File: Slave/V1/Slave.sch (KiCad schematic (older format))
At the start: 0 parts

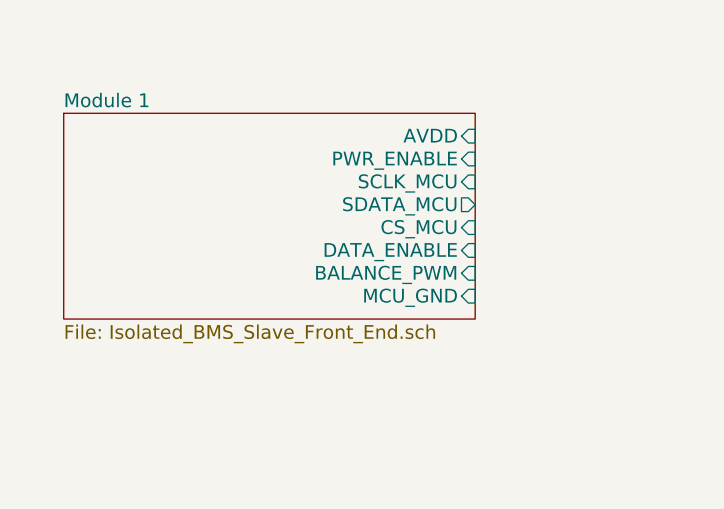
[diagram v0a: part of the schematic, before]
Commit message: add LED to reverse protection + balancing
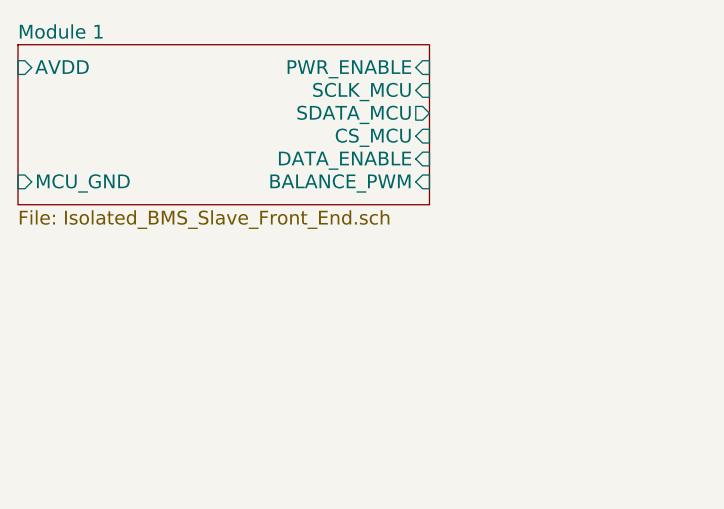
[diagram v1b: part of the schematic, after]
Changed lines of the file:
@@
 	8700 6400 9000 6400
 $Sheet
-S 800  900  1800 900
+S 600  600  1800 700
 U 5938E2BF
 F0 "Module 1" 60
 F1 "Isolated_BMS_Slave_Front_End.sch" 60
-F2 "PWR_ENABLE" I R 2600 1100 60
-F3 "SCLK_MCU" I R 2600 1200 60
-F4 "CS_MCU" I R 2600 1400 60
-F5 "BALANCE_PWM" I R 2600 1600 60
-F6 "SDATA_MCU" O R 2600 1300 60
-F7 "MCU_GND" I R 2600 1700 60
-F8 "DATA_ENABLE" I R 2600 1500 60
-F9 "AVDD" I R 2600 1000 60
+F2 "PWR_ENABLE" I R 2400 700 60
+F3 "SCLK_MCU" I R 2400 800 60
+F4 "CS_MCU" I R 2400 1000 60
+F5 "BALANCE_PWM" I R 2400 1200 60
+F6 "SDATA_MCU" O R 2400 900 60
+F7 "MCU_GND" I L 600 1200 60
+F8 "DATA_ENABLE" I R 2400 1100 60
+F9 "AVDD" I L 600 700 60
 $EndSheet
 $EndSCHEMATC

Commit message: placing components
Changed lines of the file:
@@
 F5 "BALANCE_PWM" I R 2400 1200 60
 F6 "SDATA_MCU" O R 2400 900 60
-F7 "MCU_GND" I L 600 1200 60
-F8 "DATA_ENABLE" I R 2400 1100 60
-F9 "AVDD" I L 600 700 60
+F7 "DATA_ENABLE" I R 2400 1100 60
+F8 "AVDD" I L 600 700 60
+F9 "AGND" I L 600 1200 60
 $EndSheet
 $EndSCHEMATC

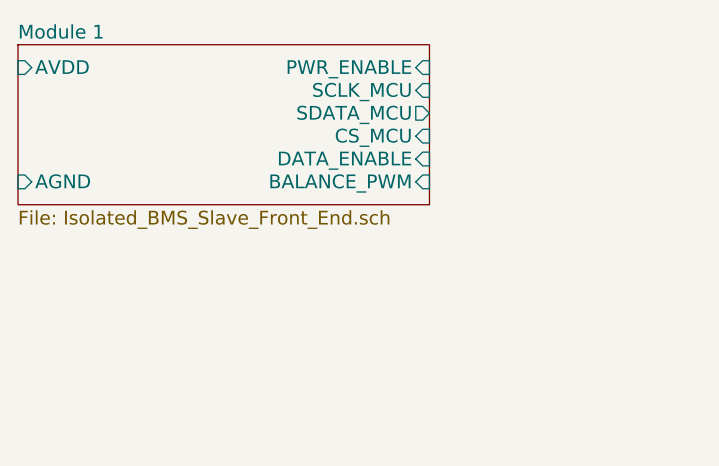
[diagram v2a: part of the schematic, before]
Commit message: placing component on front end
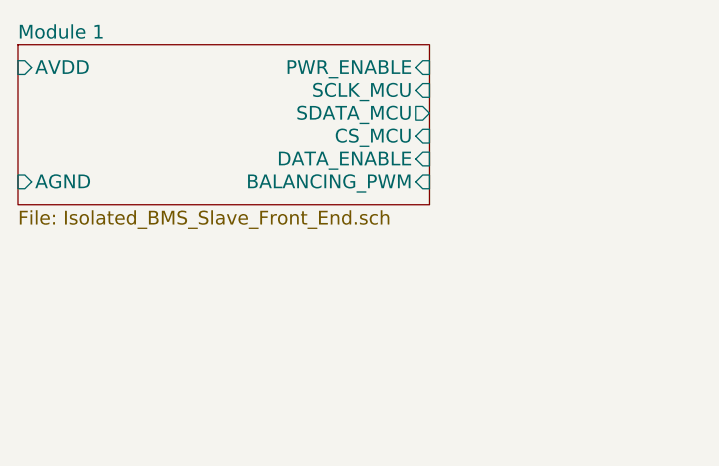
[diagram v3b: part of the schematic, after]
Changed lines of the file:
@@
 F3 "SCLK_MCU" I R 2400 800 60
 F4 "CS_MCU" I R 2400 1000 60
-F5 "BALANCE_PWM" I R 2400 1200 60
+F5 "BALANCING_PWM" I R 2400 1200 60
 F6 "SDATA_MCU" O R 2400 900 60
 F7 "DATA_ENABLE" I R 2400 1100 60

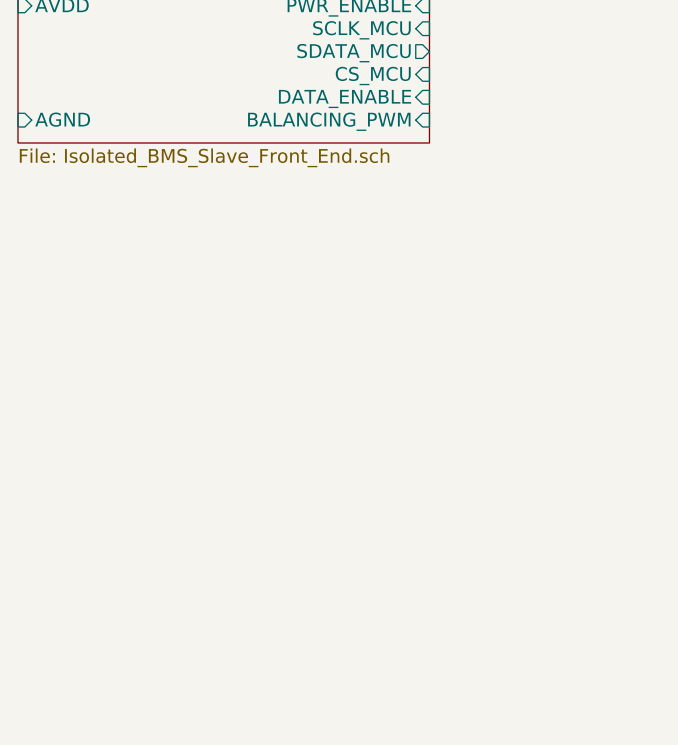
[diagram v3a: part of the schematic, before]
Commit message: adding 8 front end
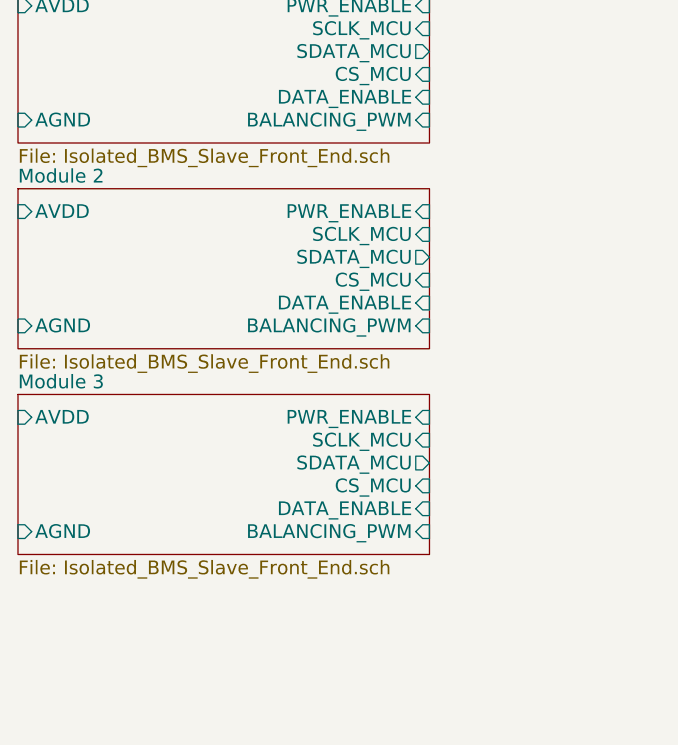
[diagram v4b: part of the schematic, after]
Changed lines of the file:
@@
 $Descr USLetter 11000 8500
 encoding utf-8
-Sheet 1 8
+Sheet 1 16
 Title ""
 Date ""
@@
 F9 "AGND" I L 600 1200 60
 $EndSheet
+$Sheet
+S 600  1500 1800 700
+U 593F9F72
+F0 "Module 2" 60
+F1 "Isolated_BMS_Slave_Front_End.sch" 60
+F2 "PWR_ENABLE" I R 2400 1600 60
+F3 "SCLK_MCU" I R 2400 1700 60
+F4 "CS_MCU" I R 2400 1900 60
+F5 "BALANCING_PWM" I R 2400 2100 60
+F6 "SDATA_MCU" O R 2400 1800 60
+F7 "DATA_ENABLE" I R 2400 2000 60
+F8 "AVDD" I L 600 1600 60
+F9 "AGND" I L 600 2100 60
+$EndSheet
+$Sheet
+S 600  2400 1800 700
+U 593FDFB1
+F0 "Module 3" 60
+F1 "Isolated_BMS_Slave_Front_End.sch" 60
+F2 "PWR_ENABLE" I R 2400 2500 60
+F3 "SCLK_MCU" I R 2400 2600 60
+F4 "CS_MCU" I R 2400 2800 60
+F5 "BALANCING_PWM" I R 2400 3000 60
+F6 "SDATA_MCU" O R 2400 2700 60
+F7 "DATA_ENABLE" I R 2400 2900 60
+F8 "AVDD" I L 600 2500 60
+F9 "AGND" I L 600 3000 60
+$EndSheet
 $EndSCHEMATC

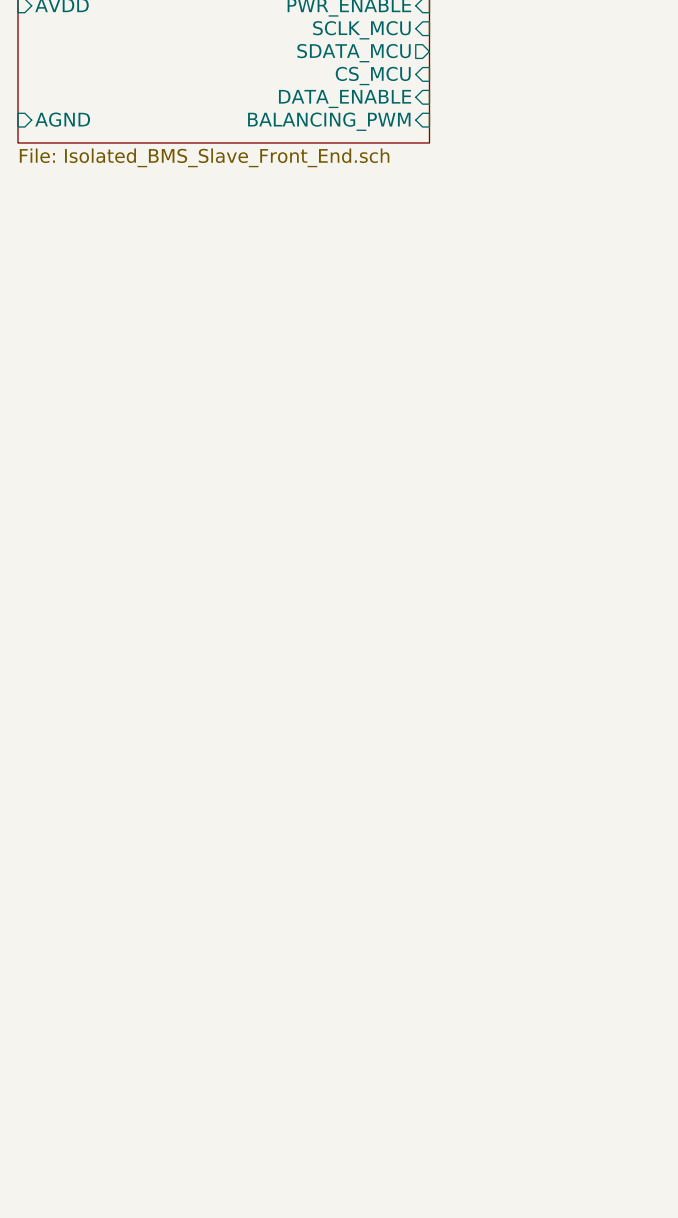
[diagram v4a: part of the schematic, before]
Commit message: placed front end 1 to 5
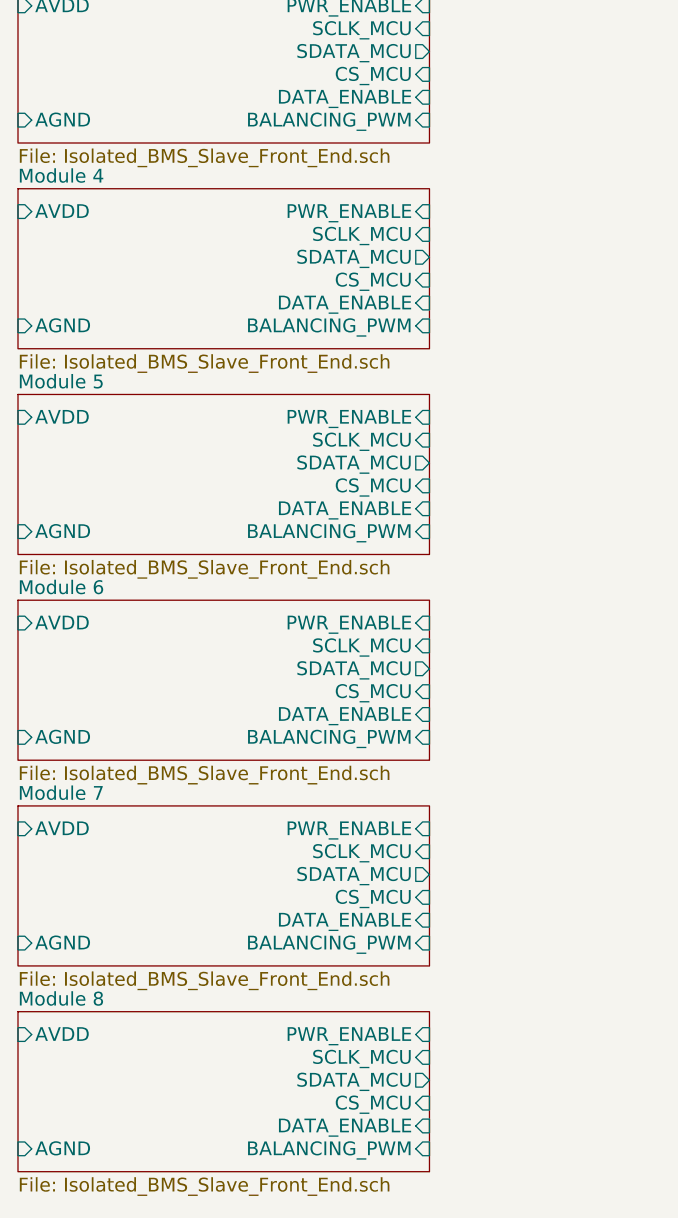
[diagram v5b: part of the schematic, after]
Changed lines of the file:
@@
 $Descr USLetter 11000 8500
 encoding utf-8
-Sheet 1 16
+Sheet 1 36
 Title ""
 Date ""
@@
 F9 "AGND" I L 600 3000 60
 $EndSheet
+$Sheet
+S 600  3300 1800 700
+U 593FF1B1
+F0 "Module 4" 60
+F1 "Isolated_BMS_Slave_Front_End.sch" 60
+F2 "PWR_ENABLE" I R 2400 3400 60
+F3 "SCLK_MCU" I R 2400 3500 60
+F4 "CS_MCU" I R 2400 3700 60
+F5 "BALANCING_PWM" I R 2400 3900 60
+F6 "SDATA_MCU" O R 2400 3600 60
+F7 "DATA_ENABLE" I R 2400 3800 60
+F8 "AVDD" I L 600 3400 60
+F9 "AGND" I L 600 3900 60
+$EndSheet
+$Sheet
+S 600  4200 1800 700
+U 593FF93E
+F0 "Module 5" 60
+F1 "Isolated_BMS_Slave_Front_End.sch" 60
+F2 "PWR_ENABLE" I R 2400 4300 60
+F3 "SCLK_MCU" I R 2400 4400 60
+F4 "CS_MCU" I R 2400 4600 60
+F5 "BALANCING_PWM" I R 2400 4800 60
+F6 "SDATA_MCU" O R 2400 4500 60
+F7 "DATA_ENABLE" I R 2400 4700 60
+F8 "AVDD" I L 600 4300 60
+F9 "AGND" I L 600 4800 60
+$EndSheet
+$Sheet
+S 600  5100 1800 700
+U 59400152
+F0 "Module 6" 60
+F1 "Isolated_BMS_Slave_Front_End.sch" 60
+F2 "PWR_ENABLE" I R 2400 5200 60
+F3 "SCLK_MCU" I R 2400 5300 60
+F4 "CS_MCU" I R 2400 5500 60
+F5 "BALANCING_PWM" I R 2400 5700 60
+F6 "SDATA_MCU" O R 2400 5400 60
+F7 "DATA_ENABLE" I R 2400 5600 60
+F8 "AVDD" I L 600 5200 60
+F9 "AGND" I L 600 5700 60
+$EndSheet
+$Sheet
+S 600  6000 1800 700
+U 59400D56
+F0 "Module 7" 60
+F1 "Isolated_BMS_Slave_Front_End.sch" 60
+F2 "PWR_ENABLE" I R 2400 6100 60
+F3 "SCLK_MCU" I R 2400 6200 60
+F4 "CS_MCU" I R 2400 6400 60
+F5 "BALANCING_PWM" I R 2400 6600 60
+F6 "SDATA_MCU" O R 2400 6300 60
+F7 "DATA_ENABLE" I R 2400 6500 60
+F8 "AVDD" I L 600 6100 60
+F9 "AGND" I L 600 6600 60
+$EndSheet
+$Sheet
+S 600  6900 1800 700
+U 59400D60
+F0 "Module 8" 60
+F1 "Isolated_BMS_Slave_Front_End.sch" 60
+F2 "PWR_ENABLE" I R 2400 7000 60
+F3 "SCLK_MCU" I R 2400 7100 60
+F4 "CS_MCU" I R 2400 7300 60
+F5 "BALANCING_PWM" I R 2400 7500 60
+F6 "SDATA_MCU" O R 2400 7200 60
+F7 "DATA_ENABLE" I R 2400 7400 60
+F8 "AVDD" I L 600 7000 60
+F9 "AGND" I L 600 7500 60
+$EndSheet
 $EndSCHEMATC

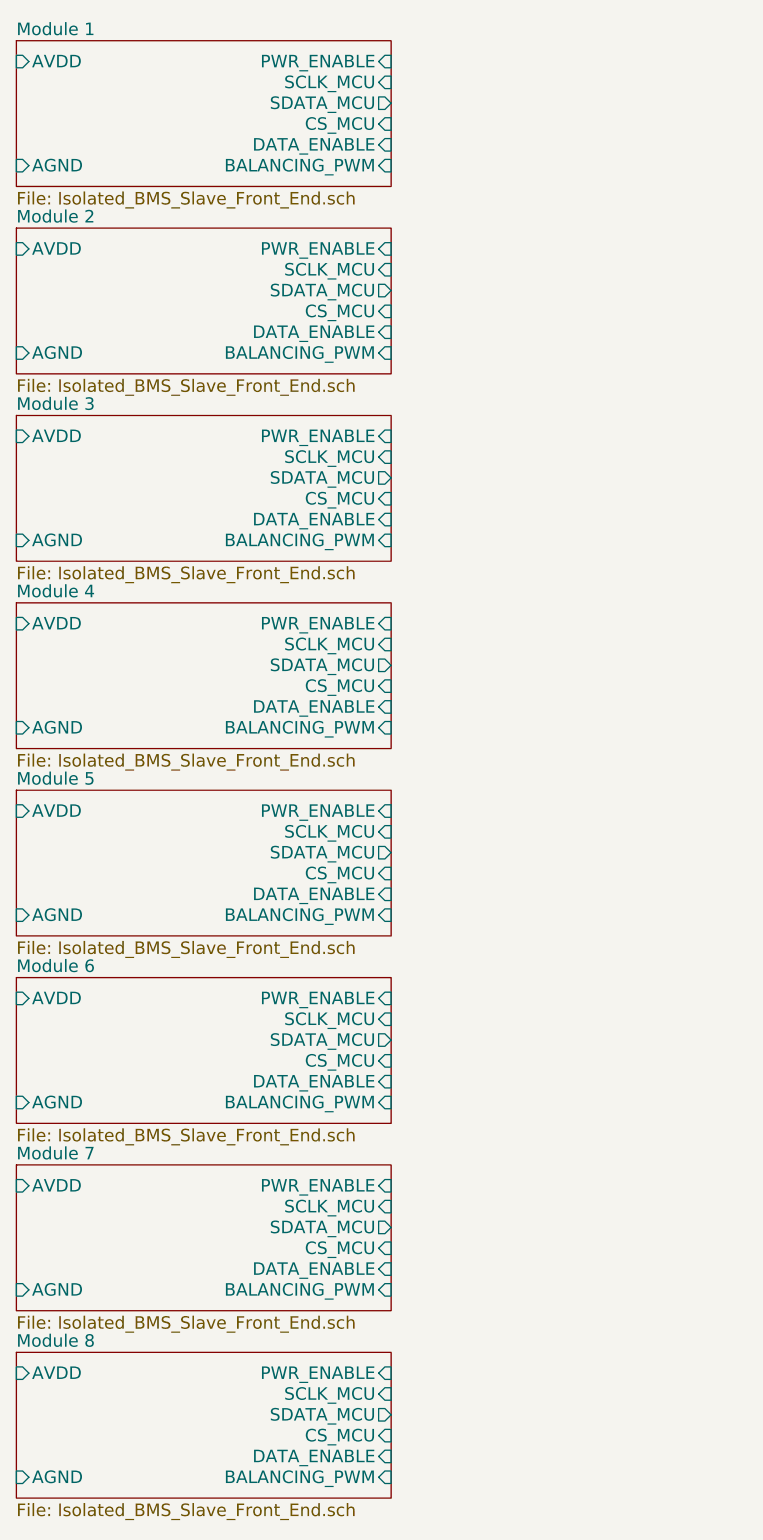
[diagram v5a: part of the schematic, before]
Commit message: place connector
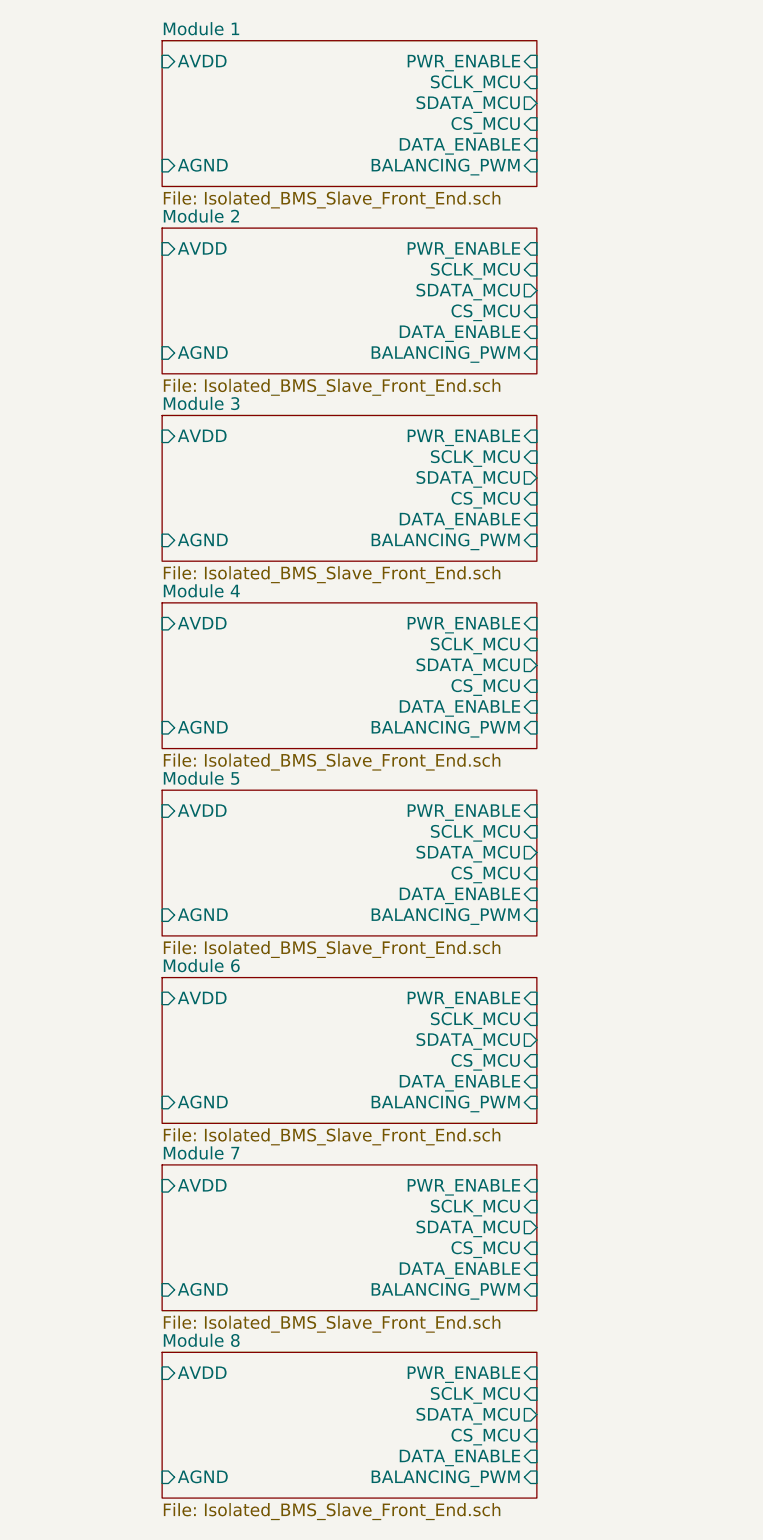
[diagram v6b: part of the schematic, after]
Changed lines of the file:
@@
 	8700 6400 9000 6400
 $Sheet
-S 600  600  1800 700
+S 1300 600  1800 700
 U 5938E2BF
 F0 "Module 1" 60
 F1 "Isolated_BMS_Slave_Front_End.sch" 60
-F2 "PWR_ENABLE" I R 2400 700 60
-F3 "SCLK_MCU" I R 2400 800 60
-F4 "CS_MCU" I R 2400 1000 60
-F5 "BALANCING_PWM" I R 2400 1200 60
-F6 "SDATA_MCU" O R 2400 900 60
-F7 "DATA_ENABLE" I R 2400 1100 60
-F8 "AVDD" I L 600 700 60
-F9 "AGND" I L 600 1200 60
+F2 "PWR_ENABLE" I R 3100 700 60
+F3 "SCLK_MCU" I R 3100 800 60
+F4 "CS_MCU" I R 3100 1000 60
+F5 "BALANCING_PWM" I R 3100 1200 60
+F6 "SDATA_MCU" O R 3100 900 60
+F7 "DATA_ENABLE" I R 3100 1100 60
+F8 "AVDD" I L 1300 700 60
+F9 "AGND" I L 1300 1200 60
 $EndSheet
 $Sheet
-S 600  1500 1800 700
+S 1300 1500 1800 700
 U 593F9F72
 F0 "Module 2" 60
 F1 "Isolated_BMS_Slave_Front_End.sch" 60
-F2 "PWR_ENABLE" I R 2400 1600 60
-F3 "SCLK_MCU" I R 2400 1700 60
-F4 "CS_MCU" I R 2400 1900 60
-F5 "BALANCING_PWM" I R 2400 2100 60
-F6 "SDATA_MCU" O R 2400 1800 60
-F7 "DATA_ENABLE" I R 2400 2000 60
-F8 "AVDD" I L 600 1600 60
-F9 "AGND" I L 600 2100 60
+F2 "PWR_ENABLE" I R 3100 1600 60
+F3 "SCLK_MCU" I R 3100 1700 60
+F4 "CS_MCU" I R 3100 1900 60
+F5 "BALANCING_PWM" I R 3100 2100 60
+F6 "SDATA_MCU" O R 3100 1800 60
+F7 "DATA_ENABLE" I R 3100 2000 60
+F8 "AVDD" I L 1300 1600 60
+F9 "AGND" I L 1300 2100 60
 $EndSheet
 $Sheet
-S 600  2400 1800 700
+S 1300 2400 1800 700
 U 593FDFB1
 F0 "Module 3" 60
 F1 "Isolated_BMS_Slave_Front_End.sch" 60
-F2 "PWR_ENABLE" I R 2400 2500 60
-F3 "SCLK_MCU" I R 2400 2600 60
-F4 "CS_MCU" I R 2400 2800 60
-F5 "BALANCING_PWM" I R 2400 3000 60
-F6 "SDATA_MCU" O R 2400 2700 60
-F7 "DATA_ENABLE" I R 2400 2900 60
-F8 "AVDD" I L 600 2500 60
-F9 "AGND" I L 600 3000 60
+F2 "PWR_ENABLE" I R 3100 2500 60
+F3 "SCLK_MCU" I R 3100 2600 60
+F4 "CS_MCU" I R 3100 2800 60
+F5 "BALANCING_PWM" I R 3100 3000 60
+F6 "SDATA_MCU" O R 3100 2700 60
+F7 "DATA_ENABLE" I R 3100 2900 60
+F8 "AVDD" I L 1300 2500 60
+F9 "AGND" I L 1300 3000 60
 $EndSheet
 $Sheet
-S 600  3300 1800 700
+S 1300 3300 1800 700
 U 593FF1B1
 F0 "Module 4" 60
 F1 "Isolated_BMS_Slave_Front_End.sch" 60
-F2 "PWR_ENABLE" I R 2400 3400 60
-F3 "SCLK_MCU" I R 2400 3500 60
-F4 "CS_MCU" I R 2400 3700 60
-F5 "BALANCING_PWM" I R 2400 3900 60
-F6 "SDATA_MCU" O R 2400 3600 60
-F7 "DATA_ENABLE" I R 2400 3800 60
-F8 "AVDD" I L 600 3400 60
-F9 "AGND" I L 600 3900 60
+F2 "PWR_ENABLE" I R 3100 3400 60
+F3 "SCLK_MCU" I R 3100 3500 60
+F4 "CS_MCU" I R 3100 3700 60
+F5 "BALANCING_PWM" I R 3100 3900 60
+F6 "SDATA_MCU" O R 3100 3600 60
+F7 "DATA_ENABLE" I R 3100 3800 60
+F8 "AVDD" I L 1300 3400 60
+F9 "AGND" I L 1300 3900 60
 $EndSheet
 $Sheet
-S 600  4200 1800 700
+S 1300 4200 1800 700
 U 593FF93E
 F0 "Module 5" 60
 F1 "Isolated_BMS_Slave_Front_End.sch" 60
-F2 "PWR_ENABLE" I R 2400 4300 60
-F3 "SCLK_MCU" I R 2400 4400 60
-F4 "CS_MCU" I R 2400 4600 60
-F5 "BALANCING_PWM" I R 2400 4800 60
-F6 "SDATA_MCU" O R 2400 4500 60
-F7 "DATA_ENABLE" I R 2400 4700 60
-F8 "AVDD" I L 600 4300 60
-F9 "AGND" I L 600 4800 60
+F2 "PWR_ENABLE" I R 3100 4300 60
+F3 "SCLK_MCU" I R 3100 4400 60
+F4 "CS_MCU" I R 3100 4600 60
+F5 "BALANCING_PWM" I R 3100 4800 60
+F6 "SDATA_MCU" O R 3100 4500 60
+F7 "DATA_ENABLE" I R 3100 4700 60
+F8 "AVDD" I L 1300 4300 60
+F9 "AGND" I L 1300 4800 60
 $EndSheet
 $Sheet
-S 600  5100 1800 700
+S 1300 5100 1800 700
 U 59400152
 F0 "Module 6" 60
 F1 "Isolated_BMS_Slave_Front_End.sch" 60
-F2 "PWR_ENABLE" I R 2400 5200 60
-F3 "SCLK_MCU" I R 2400 5300 60
-F4 "CS_MCU" I R 2400 5500 60
-F5 "BALANCING_PWM" I R 2400 5700 60
-F6 "SDATA_MCU" O R 2400 5400 60
-F7 "DATA_ENABLE" I R 2400 5600 60
-F8 "AVDD" I L 600 5200 60
-F9 "AGND" I L 600 5700 60
+F2 "PWR_ENABLE" I R 3100 5200 60
+F3 "SCLK_MCU" I R 3100 5300 60
+F4 "CS_MCU" I R 3100 5500 60
+F5 "BALANCING_PWM" I R 3100 5700 60
+F6 "SDATA_MCU" O R 3100 5400 60
+F7 "DATA_ENABLE" I R 3100 5600 60
+F8 "AVDD" I L 1300 5200 60
+F9 "AGND" I L 1300 5700 60
 $EndSheet
 $Sheet
-S 600  6000 1800 700
+S 1300 6000 1800 700
 U 59400D56
 F0 "Module 7" 60
 F1 "Isolated_BMS_Slave_Front_End.sch" 60
-F2 "PWR_ENABLE" I R 2400 6100 60
-F3 "SCLK_MCU" I R 2400 6200 60
-F4 "CS_MCU" I R 2400 6400 60
-F5 "BALANCING_PWM" I R 2400 6600 60
-F6 "SDATA_MCU" O R 2400 6300 60
-F7 "DATA_ENABLE" I R 2400 6500 60
-F8 "AVDD" I L 600 6100 60
-F9 "AGND" I L 600 6600 60
+F2 "PWR_ENABLE" I R 3100 6100 60
+F3 "SCLK_MCU" I R 3100 6200 60
+F4 "CS_MCU" I R 3100 6400 60
+F5 "BALANCING_PWM" I R 3100 6600 60
+F6 "SDATA_MCU" O R 3100 6300 60
+F7 "DATA_ENABLE" I R 3100 6500 60
+F8 "AVDD" I L 1300 6100 60
+F9 "AGND" I L 1300 6600 60
 $EndSheet
 $Sheet
-S 600  6900 1800 700
+S 1300 6900 1800 700
 U 59400D60
 F0 "Module 8" 60
 F1 "Isolated_BMS_Slave_Front_End.sch" 60
-F2 "PWR_ENABLE" I R 2400 7000 60
-F3 "SCLK_MCU" I R 2400 7100 60
-F4 "CS_MCU" I R 2400 7300 60
-F5 "BALANCING_PWM" I R 2400 7500 60
-F6 "SDATA_MCU" O R 2400 7200 60
-F7 "DATA_ENABLE" I R 2400 7400 60
-F8 "AVDD" I L 600 7000 60
-F9 "AGND" I L 600 7500 60
+F2 "PWR_ENABLE" I R 3100 7000 60
+F3 "SCLK_MCU" I R 3100 7100 60
+F4 "CS_MCU" I R 3100 7300 60
+F5 "BALANCING_PWM" I R 3100 7500 60
+F6 "SDATA_MCU" O R 3100 7200 60
+F7 "DATA_ENABLE" I R 3100 7400 60
+F8 "AVDD" I L 1300 7000 60
+F9 "AGND" I L 1300 7500 60
 $EndSheet
 $EndSCHEMATC
